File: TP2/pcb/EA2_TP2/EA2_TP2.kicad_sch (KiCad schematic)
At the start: 33 parts, among them U1 TL082, U2 TL082, U3 TL082, U4 TL082

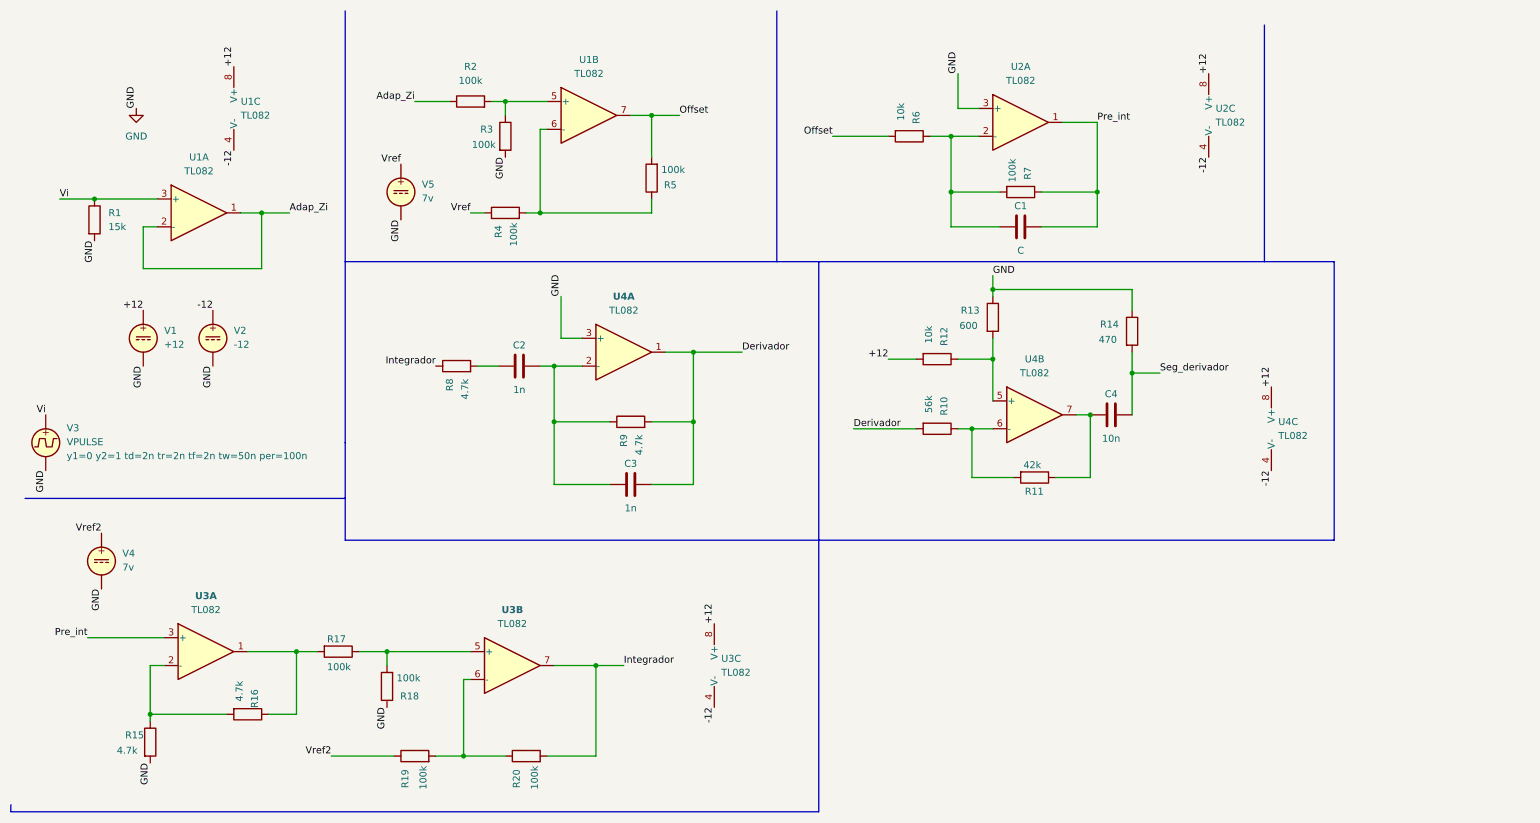
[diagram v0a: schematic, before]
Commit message: resistencias normalizadas y div r, footprints
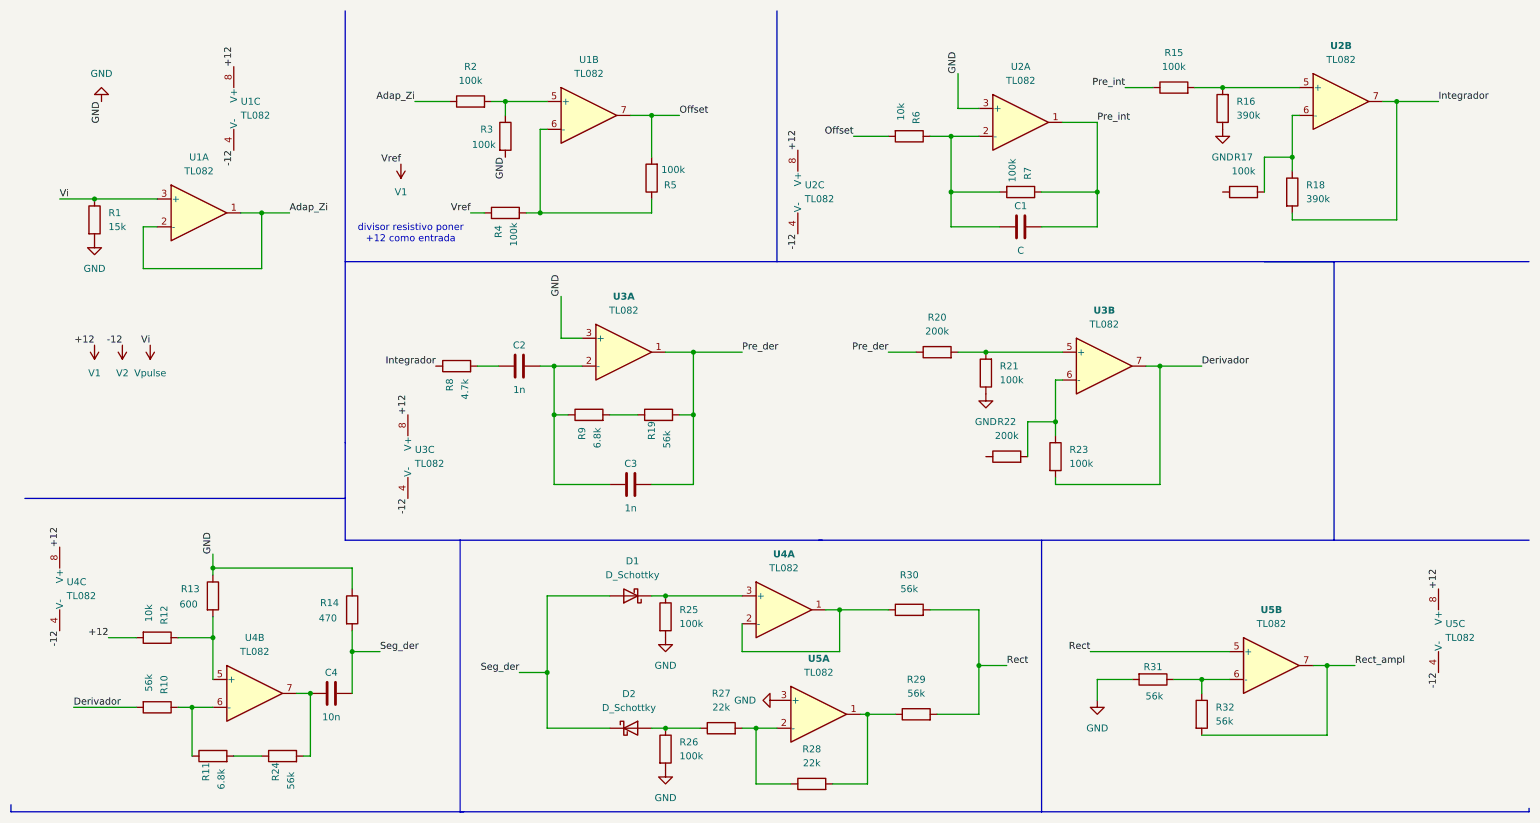
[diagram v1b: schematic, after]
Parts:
- removed unit 1 of U3
- removed unit 3 of U3
- removed V1: +12, symbol Simulation_SPICE:VDC
- removed V2: -12, symbol Simulation_SPICE:VDC
- removed V3: VPULSE, symbol Simulation_SPICE:VPULSE
- removed V4, V5: 7v, symbol Simulation_SPICE:VDC
- added D1, D2: D_Schottky, Diode_THT:D_5W_P12.70mm_Horizontal, symbol Device:D_Schottky
- added R21, R23, R25, R26: 100k, Resistor_THT:R_Axial_DIN0411_L9.9mm_D3.6mm_P15.24mm_Horizontal, symbol Device:R
- added R22: 200k, Resistor_THT:R_Axial_DIN0411_L9.9mm_D3.6mm_P15.24mm_Horizontal, symbol Device:R
- added R24, R29, R30, R31, R32: 56k, Resistor_THT:R_Axial_DIN0411_L9.9mm_D3.6mm_P15.24mm_Horizontal, symbol Device:R
- added R27, R28: 22k, Resistor_THT:R_Axial_DIN0411_L9.9mm_D3.6mm_P15.24mm_Horizontal, symbol Device:R
- added unit 2 of U2
- added unit 1 of U4
- added unit 3 of U4
- added U5: TL082, Package_DIP:DIP-8_W7.62mm, symbol Amplifier_Operational:TL082
- C1, C2, C3, C4: footprint (none) -> Capacitor_THT:C_Disc_D7.0mm_W2.5mm_P5.00mm
- R1, R10, R12, R13, R14, R17, R2, R3, R4, R5, R6, R7, R8: footprint (none) -> Resistor_THT:R_Axial_DIN0411_L9.9mm_D3.6mm_P15.24mm_Horizontal
- R11: value 42k -> 6.8k; footprint (none) -> Resistor_THT:R_Axial_DIN0411_L9.9mm_D3.6mm_P15.24mm_Horizontal
- R15: value 4.7k -> 100k; footprint (none) -> Resistor_THT:R_Axial_DIN0411_L9.9mm_D3.6mm_P15.24mm_Horizontal
- R16: value 4.7k -> 390k; footprint (none) -> Resistor_THT:R_Axial_DIN0411_L9.9mm_D3.6mm_P15.24mm_Horizontal
- R18: value 100k -> 390k; footprint (none) -> Resistor_THT:R_Axial_DIN0411_L9.9mm_D3.6mm_P15.24mm_Horizontal
- R19: value 100k -> 56k; footprint (none) -> Resistor_THT:R_Axial_DIN0411_L9.9mm_D3.6mm_P15.24mm_Horizontal
- R20: value 100k -> 200k; footprint (none) -> Resistor_THT:R_Axial_DIN0411_L9.9mm_D3.6mm_P15.24mm_Horizontal
- R9: value 4.7k -> 6.8k; footprint (none) -> Resistor_THT:R_Axial_DIN0411_L9.9mm_D3.6mm_P15.24mm_Horizontal
- U1, U2, U3, U4: footprint (none) -> Package_DIP:DIP-8_W7.62mm
- U3: renamed from U4; footprint (none) -> Package_DIP:DIP-8_W7.62mm
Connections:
- net Vref is gone; now on net V1: R4.1
- net Derivador: now also U3.7, R23.2; no longer C3.1, R9.2, U3.1
- net GND: now also R16.1, R21.1, R25.2, R26.2, R31.2, U5.3 (+); no longer R15.2, R18.1
- net Integrador: now also R18.2, U2.7; no longer R20.2, U3.7
- net Pre_int: now also R15.1
- net Pre_der: now reaches R19.2, R20.1
- net Pre_der: now also C3.1, U3.1; no longer U3.6 (-)
- net at R17.2: now also R18.1, U2.6 (-); no longer R16.1
- net at R16.2: now also R15.2, U2.5 (+); no longer R15.1
- net at R10.1, U4.6 (-): now also R11.1; no longer R11.2
- net at C4.2, U4.7: now also R24.2; no longer R11.1
- net +12 renamed V1
- net V1: now also U4.8 (V+), U5.8 (V+)
- net -12 renamed V2
- net V2: now also U4.4 (V-), U5.4 (V-)
- net Seg_derivador renamed Seg_der
- net Seg_der: now also D1.2 (A), D2.1 (K)
- net Vi renamed Vpulse
- net Vref2: no longer names the net of R19.1
- net Vref2: now also R9.2
- new net: D1.1 (K), R25.1, U4.3 (+)
- new net: D2.2 (A), R26.1, R27.1
- new net: R27.2, R28.1, U5.2 (-)
- new net: R20.2, R21.2, U3.5 (+)
- new net: R28.2, R29.1, U5.1
- new net: R31.1, R32.1, U5.6 (-)
- new net: R22.2, R23.1, U3.6 (-)
- new net: R30.1, U4.1, U4.2 (-)
- new net: R11.2, R24.1
- new net Rect: R29.2, R30.2, U5.5 (+)
- new net Rect_ampl: R32.2, U5.7
- now unconnected: R17.1
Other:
- note added: "divisor resistivo poner +12 como entrada"
- moved on the sheet: C4, R10, R12, R13, R14, U2C, U3C, U4B

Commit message: version final pcb
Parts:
- added J1, J10, J2, J3, J4, J5, J6, J7, J8, J9: Conn_01x01_Pin, Connector_PinHeader_1.00mm:PinHeader_1x01_P1.00mm_Vertical, symbol Connector:Conn_01x01_Pin
- added R33: 7k, Resistor_THT:R_Axial_DIN0411_L9.9mm_D3.6mm_P15.24mm_Horizontal, symbol Device:R
- added R34, R38: 1k, Resistor_THT:R_Axial_DIN0411_L9.9mm_D3.6mm_P15.24mm_Horizontal, symbol Device:R
- added R35: 27k, Resistor_THT:R_Axial_DIN0411_L9.9mm_D3.6mm_P15.24mm_Horizontal, symbol Device:R
- added R36: 5.6k, Resistor_THT:R_Axial_DIN0411_L9.9mm_D3.6mm_P15.24mm_Horizontal, symbol Device:R
- added R37: 2.8k, Resistor_THT:R_Axial_DIN0411_L9.9mm_D3.6mm_P15.24mm_Horizontal, symbol Device:R
- C1: value C -> 10n
- C3: value 1n -> 56p
- R16, R18: value 390k -> 380k
- R25: value 100k -> 100
- R31: value 56k -> 1k
- R32: value 56k -> 380k
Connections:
- net Derivador: now also J7.1 (Pin_1)
- net GND: now also J4.1 (Pin_1), R34.2, R36.2, R38.2
- net Integrador: now also J6.1 (Pin_1)
- net Offset: now also J5.1 (Pin_1)
- net Rect: now also J9.1 (Pin_1)
- net Rect_ampl: now also J10.1 (Pin_1)
- net Seg_der: now also J8.1 (Pin_1)
- net Vref_3: now reaches R22.1
- net Vref_3: now also R37.2, R38.1
- net Vref_2: now reaches R17.1
- net Vref_2: now also R35.2, R36.1
- net V1 renamed +12
- net +12: now also J1.1 (Pin_1), R33.1, R35.1; no longer R4.1
- net V2 renamed -12
- net -12: now also J2.1 (Pin_1), R37.1
- net Vpulse renamed Vi
- net Vi: now also J3.1 (Pin_1)
- new net Vref_1: R33.2, R34.1, R4.1
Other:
- note removed: "divisor resistivo poner +12 como entrada"
- moved on the sheet: R1, U1A, U1C, U5C
